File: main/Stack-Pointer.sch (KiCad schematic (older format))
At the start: 8 parts, among them U100 74LS86, U101 74LS191, U102 74LS191, U95 74LS86, U96 74LS191, U97 74LS245, U98 74LS191, U99 74LS245

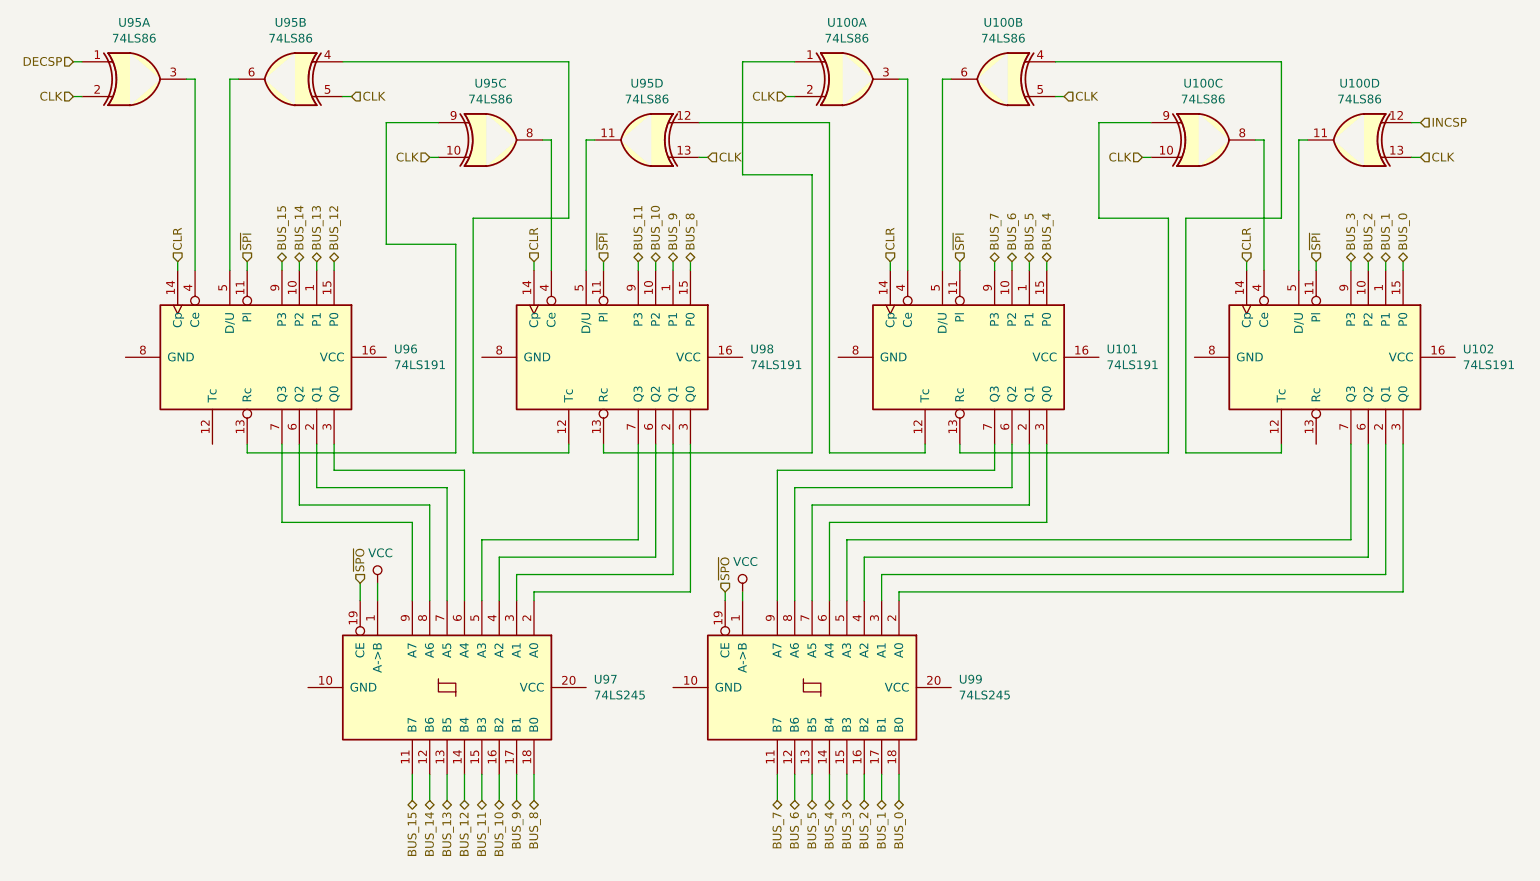
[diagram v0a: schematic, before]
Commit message: Replot main with symbols
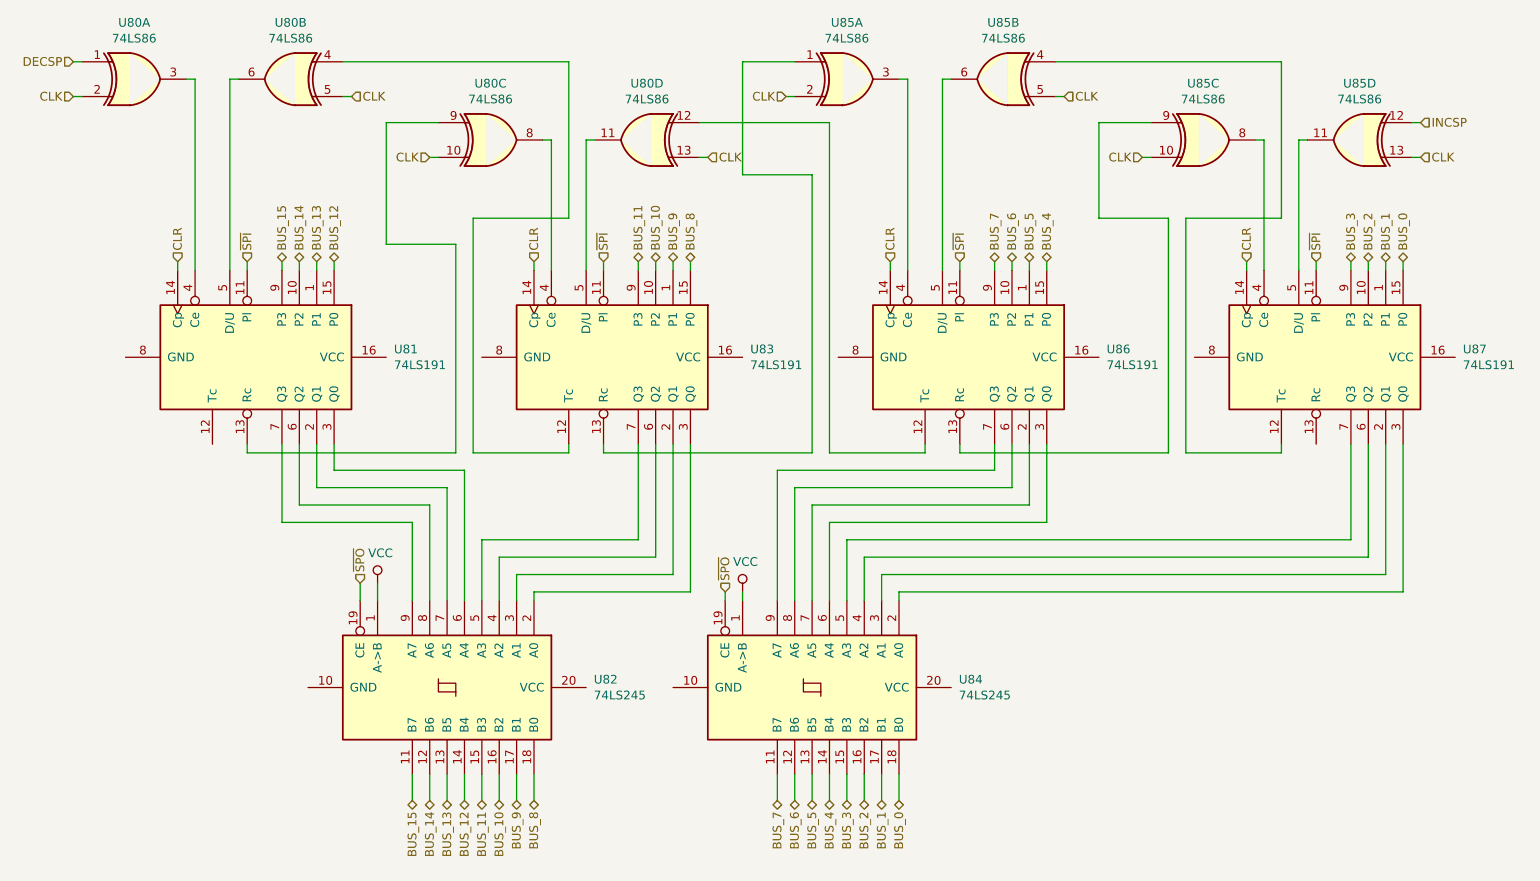
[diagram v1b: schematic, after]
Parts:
- renumbered U95 to U80, U96 to U81, U97 to U82, U98 to U83, U99 to U84, U100 to U85, U101 to U86, U102 to U87
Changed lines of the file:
@@
 Sheet 22 26
 Title "Stack Pointer"
-Date "2019-11-13"
+Date "2019-11-17"
 Rev "v1.0"
 Comp "Christopher Milan"
@@
 P 3800 5250
 AR Path="/5DA98D6D/5DA9A5CB/5DA57004" Ref="U?"  Part="1"
-AR Path="/5DA98D6D/5DA9A545/5DA57004" Ref="U97"  Part="1"
-F 0 "U97" V 3754 6094 50  0000 L CNN
+AR Path="/5DA98D6D/5DA9A545/5DA57004" Ref="U82"  Part="1"
+F 0 "U82" V 3754 6094 50  0000 L CNN
 F 1 "74LS245" V 3845 6094 50  0000 L CNN
 F 2 "" H 3800 5250 50  0001 C CNN
@@
 P 5900 5250
 AR Path="/5DA98D6D/5DA9A5CB/5DA5700A" Ref="U?"  Part="1"
-AR Path="/5DA98D6D/5DA9A545/5DA5700A" Ref="U99"  Part="1"
-F 0 "U99" V 5854 6094 50  0000 L CNN
+AR Path="/5DA98D6D/5DA9A545/5DA5700A" Ref="U84"  Part="1"
+F 0 "U84" V 5854 6094 50  0000 L CNN
 F 1 "74LS245" V 5945 6094 50  0000 L CNN
 F 2 "" H 5900 5250 50  0001 C CNN
@@
 	8400 2800 8400 2850
 $Comp
-L 74xx:74LS191 U102
+L 74xx:74LS191 U87
 U 1 1 5DB14F60
 P 8900 3350
-F 0 "U102" V 8854 4094 50  0000 L CNN
+F 0 "U87" V 8854 4094 50  0000 L CNN
 F 1 "74LS191" V 8945 4094 50  0000 L CNN
 F 2 "" H 8900 3350 50  0001 C CNN
@@
 $EndComp
 $Comp
-L 74xx:74LS191 U101
+L 74xx:74LS191 U86
 U 1 1 5DB86D50
 P 6850 3350
-F 0 "U101" V 6804 4094 50  0000 L CNN
+F 0 "U86" V 6804 4094 50  0000 L CNN
 F 1 "74LS191" V 6895 4094 50  0000 L CNN
 F 2 "" H 6850 3350 50  0001 C CNN
@@
 $EndComp
 $Comp
-L 74xx:74LS86 U100
+L 74xx:74LS86 U85
 U 4 1 5DBE960D
 P 9050 2100
-F 0 "U100" H 9050 2425 50  0000 C CNN
+F 0 "U85" H 9050 2425 50  0000 C CNN
 F 1 "74LS86" H 9050 2334 50  0000 C CNN
 F 2 "" H 9050 2100 50  0001 C CNN
@@
 	8700 2100 8750 2100
 $Comp
-L 74xx:74LS86 U100
+L 74xx:74LS86 U85
 U 3 1 5DB27703
 P 8150 2100
-F 0 "U100" H 8150 2425 50  0000 C CNN
+F 0 "U85" H 8150 2425 50  0000 C CNN
 F 1 "74LS86" H 8150 2334 50  0000 C CNN
 F 2 "" H 8150 2100 50  0001 C CNN
@@
 	7800 2200 7850 2200
 $Comp
-L 74xx:74LS86 U100
+L 74xx:74LS86 U85
 U 2 1 5DC447D6
 P 7000 1750
-F 0 "U100" H 7000 2075 50  0000 C CNN
+F 0 "U85" H 7000 2075 50  0000 C CNN
 F 1 "74LS86" H 7000 1984 50  0000 C CNN
 F 2 "" H 7000 1750 50  0001 C CNN
@@
 	6650 1750 6700 1750
 $Comp
-L 74xx:74LS86 U100
+L 74xx:74LS86 U85
 U 1 1 5DC447DF
 P 6100 1750
-F 0 "U100" H 6100 2075 50  0000 C CNN
+F 0 "U85" H 6100 2075 50  0000 C CNN
 F 1 "74LS86" H 6100 1984 50  0000 C CNN
 F 2 "" H 6100 1750 50  0001 C CNN
@@
 	8600 3900 8050 3900
 $Comp
-L 74xx:74LS191 U98
+L 74xx:74LS191 U83
 U 1 1 5DCAEED0
 P 4800 3350
-F 0 "U98" V 4754 4094 50  0000 L CNN
+F 0 "U83" V 4754 4094 50  0000 L CNN
 F 1 "74LS191" V 4845 4094 50  0000 L CNN
 F 2 "" H 4800 3350 50  0001 C CNN
@@
 	5500 1650 5800 1650
 $Comp
-L 74xx:74LS86 U95
+L 74xx:74LS86 U80
 U 4 1 5DD0CA8A
 P 4950 2100
-F 0 "U95" H 4950 2425 50  0000 C CNN
+F 0 "U80" H 4950 2425 50  0000 C CNN
 F 1 "74LS86" H 4950 2334 50  0000 C CNN
 F 2 "" H 4950 2100 50  0001 C CNN
@@
 	4600 2100 4650 2100
 $Comp
-L 74xx:74LS86 U95
+L 74xx:74LS86 U80
 U 3 1 5DD0CA93
 P 4050 2100
-F 0 "U95" H 4050 2425 50  0000 C CNN
+F 0 "U80" H 4050 2425 50  0000 C CNN
 F 1 "74LS86" H 4050 2334 50  0000 C CNN
 F 2 "" H 4050 2100 50  0001 C CNN
@@
 	5250 2000 6000 2000
 $Comp
-L 74xx:74LS191 U96
+L 74xx:74LS191 U81
 U 1 1 5DD1D569
 P 2750 3350
-F 0 "U96" V 2704 4094 50  0000 L CNN
+F 0 "U81" V 2704 4094 50  0000 L CNN
 F 1 "74LS191" V 2795 4094 50  0000 L CNN
 F 2 "" H 2750 3350 50  0001 C CNN
@@
 DECSP
 $Comp
-L 74xx:74LS86 U95
+L 74xx:74LS86 U80
 U 2 1 5DD38B59
 P 2900 1750
-F 0 "U95" H 2900 2075 50  0000 C CNN
+F 0 "U80" H 2900 2075 50  0000 C CNN
 F 1 "74LS86" H 2900 1984 50  0000 C CNN
 F 2 "" H 2900 1750 50  0001 C CNN
@@
 	1650 1650 1700 1650
 $Comp
-L 74xx:74LS86 U95
+L 74xx:74LS86 U80
 U 1 1 5DD38B62
 P 2000 1750
-F 0 "U95" H 2000 2075 50  0000 C CNN
+F 0 "U80" H 2000 2075 50  0000 C CNN
 F 1 "74LS86" H 2000 1984 50  0000 C CNN
 F 2 "" H 2000 1750 50  0001 C CNN
